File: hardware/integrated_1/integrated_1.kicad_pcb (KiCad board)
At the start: 4 copper layers, 40 x 100 mm, 84 parts, among them J1 USB4105-GF-A-120, J2 HDMI_A_1.4, SW1 DNF, SW2 DNF, U1 XC6SLX9-TQG144, U2 W25Q16JV, U3 RP2040, U5 TPS650250RHBR, Y1 12MHz

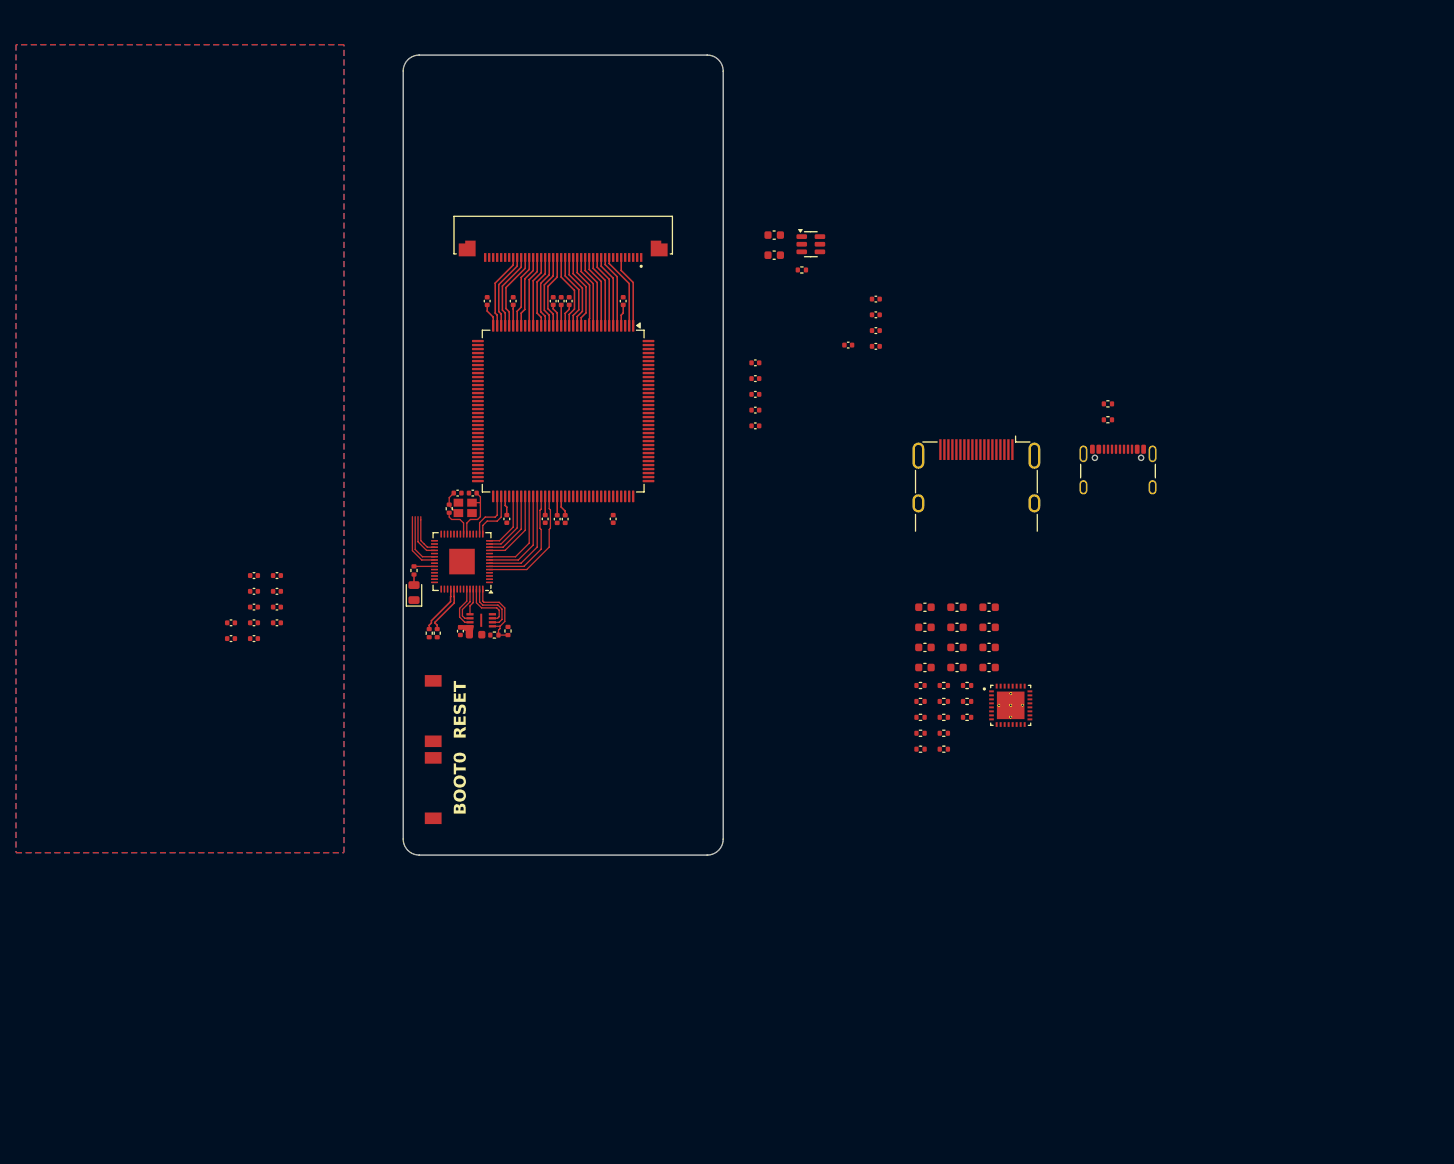
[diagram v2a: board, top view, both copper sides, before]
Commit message: started the layout process + added new hdmi and usb connectors
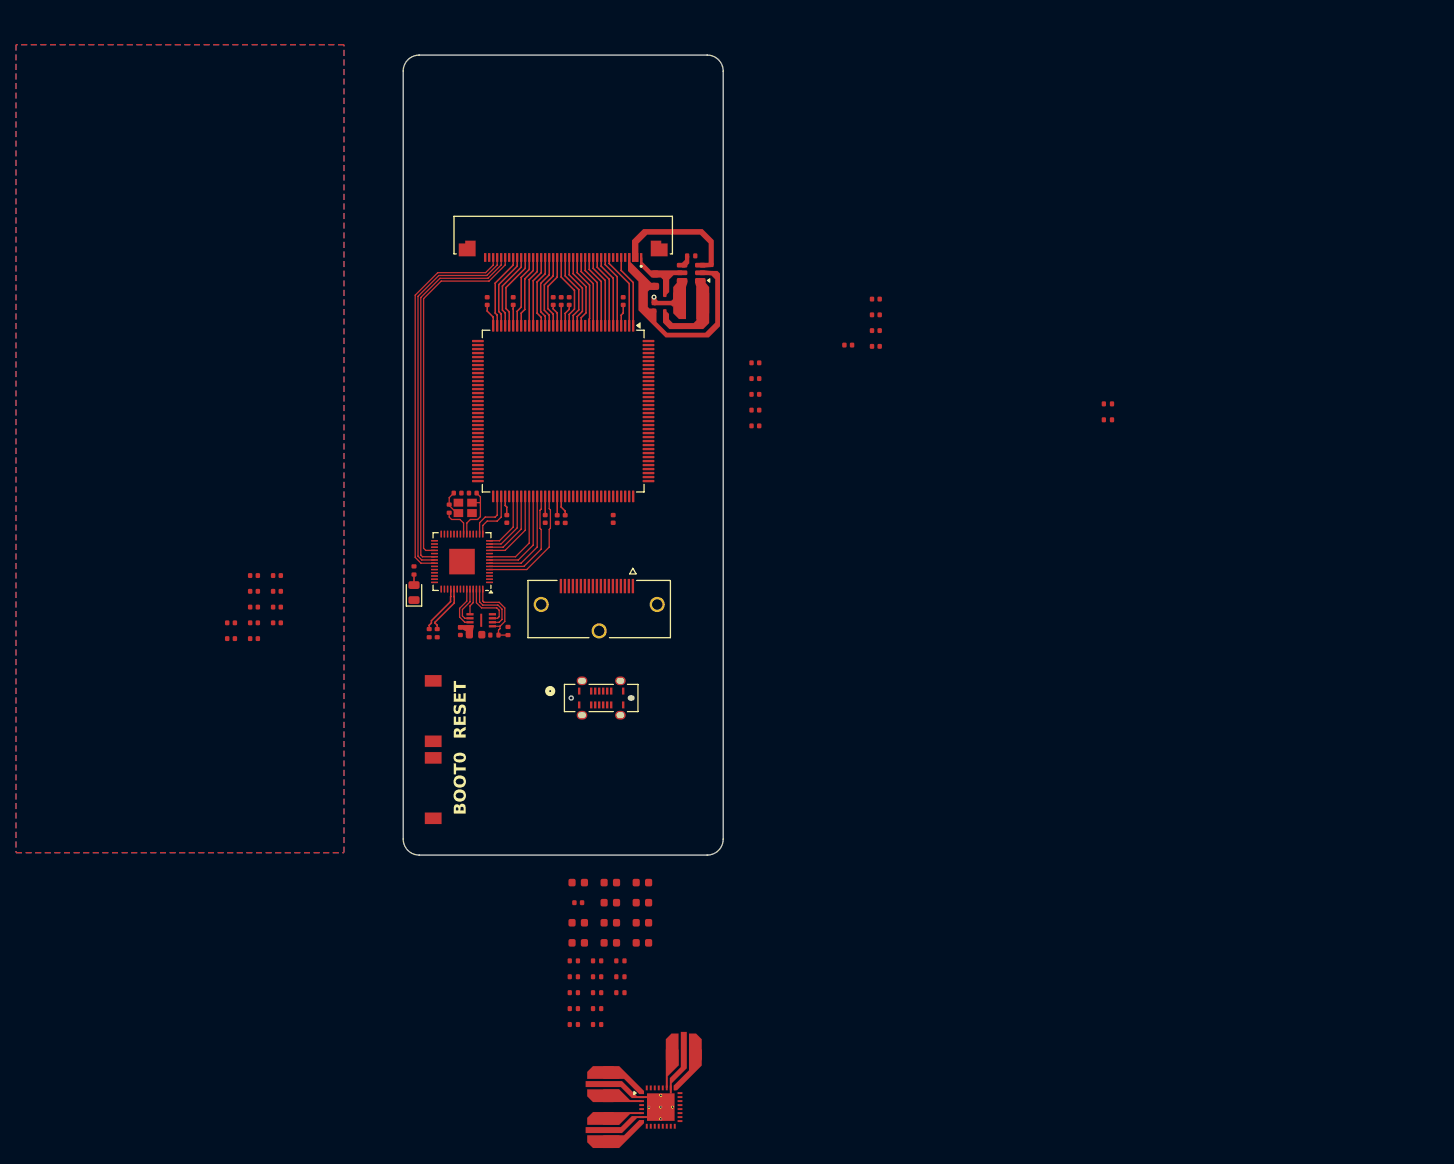
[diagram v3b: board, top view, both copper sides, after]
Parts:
- added D2: ZLLS400TA, Diode_SMD:D_SOD-323, F.Cu at (158.7, 76.5)
- added L1: 22u, KiCAD Library:XRNR4012, F.Cu at (162.0, 76.5)
- added L2: 2u2, KiCAD Library:XRNR4012, F.Cu at (151.0, 179.9)
- added L3: 3u3, KiCAD Library:XRNR4012, F.Cu at (161.1, 169.8)
- added L4: 2u2, KiCAD Library:XRNR4012, F.Cu at (151.0, 174.1)
- added R9: 100, KiCAD Library:R_0402_1005Metric, F.Cu at (162.0, 70.6)
- C1: renamed from C54; footprint Capacitor_SMD:C_0402_1005Metric -> KiCAD Library:C_0402_1005Metric
- C10: renamed from C63; footprint Capacitor_SMD:C_0402_1005Metric -> KiCAD Library:C_0402_1005Metric
- C11: renamed from C1; footprint Capacitor_SMD:C_0402_1005Metric -> KiCAD Library:C_0402_1005Metric
- C12: renamed from C2; footprint Capacitor_SMD:C_0402_1005Metric -> KiCAD Library:C_0402_1005Metric
- C13: renamed from C3; footprint Capacitor_SMD:C_0402_1005Metric -> KiCAD Library:C_0402_1005Metric
- C14: renamed from C4; footprint Capacitor_SMD:C_0402_1005Metric -> KiCAD Library:C_0402_1005Metric
- C15: renamed from C5; footprint Capacitor_SMD:C_0402_1005Metric -> KiCAD Library:C_0402_1005Metric
- C16: renamed from C6; footprint Capacitor_SMD:C_0402_1005Metric -> KiCAD Library:C_0402_1005Metric
- C17: renamed from C7; footprint Capacitor_SMD:C_0402_1005Metric -> KiCAD Library:C_0402_1005Metric
- C18: renamed from C8; footprint Capacitor_SMD:C_0402_1005Metric -> KiCAD Library:C_0402_1005Metric
- C19: renamed from C9; footprint Capacitor_SMD:C_0402_1005Metric -> KiCAD Library:C_0402_1005Metric
- C2: renamed from C55; footprint Capacitor_SMD:C_0402_1005Metric -> KiCAD Library:C_0402_1005Metric
- C20: renamed from C10; footprint Capacitor_SMD:C_0402_1005Metric -> KiCAD Library:C_0402_1005Metric
- C21: renamed from C11; footprint Capacitor_SMD:C_0402_1005Metric -> KiCAD Library:C_0402_1005Metric
- C22: renamed from C12; footprint Capacitor_SMD:C_0402_1005Metric -> KiCAD Library:C_0402_1005Metric
- C23: renamed from C13; footprint Capacitor_SMD:C_0402_1005Metric -> KiCAD Library:C_0402_1005Metric
- C24: renamed from C14; footprint Capacitor_SMD:C_0402_1005Metric -> KiCAD Library:C_0402_1005Metric
- C26: renamed from C16; footprint Capacitor_SMD:C_0402_1005Metric -> KiCAD Library:C_0402_1005Metric
- C27: renamed from C17; footprint Capacitor_SMD:C_0402_1005Metric -> KiCAD Library:C_0402_1005Metric
- C28: renamed from C18; footprint Capacitor_SMD:C_0402_1005Metric -> KiCAD Library:C_0402_1005Metric
- C29: renamed from C19; footprint Capacitor_SMD:C_0402_1005Metric -> KiCAD Library:C_0402_1005Metric
- C3: renamed from C56; footprint Capacitor_SMD:C_0402_1005Metric -> KiCAD Library:C_0402_1005Metric
- C30: renamed from C20; footprint Capacitor_SMD:C_0402_1005Metric -> KiCAD Library:C_0402_1005Metric
- C31: renamed from C21; footprint Capacitor_SMD:C_0402_1005Metric -> KiCAD Library:C_0402_1005Metric
- C32: renamed from C22; footprint Capacitor_SMD:C_0402_1005Metric -> KiCAD Library:C_0402_1005Metric
- C33: renamed from C23; footprint Capacitor_SMD:C_0402_1005Metric -> KiCAD Library:C_0402_1005Metric
- C34: renamed from C24; footprint Capacitor_SMD:C_0402_1005Metric -> KiCAD Library:C_0402_1005Metric
- C35: renamed from C25; footprint Capacitor_SMD:C_0402_1005Metric -> KiCAD Library:C_0402_1005Metric
- C36: renamed from C26; footprint Capacitor_SMD:C_0402_1005Metric -> KiCAD Library:C_0402_1005Metric
- C37: renamed from C27; footprint Capacitor_SMD:C_0603_1608Metric -> KiCAD Library:C_0402_1005Metric
- C38: renamed from C28; footprint Capacitor_SMD:C_0603_1608Metric -> KiCAD Library:C_0603_1608Metric
- C39: renamed from C29; footprint Capacitor_SMD:C_0603_1608Metric -> KiCAD Library:C_0603_1608Metric
- C4: renamed from C57; footprint Capacitor_SMD:C_0402_1005Metric -> KiCAD Library:C_0402_1005Metric
- C40: renamed from C30; footprint Capacitor_SMD:C_0603_1608Metric -> KiCAD Library:C_0402_1005Metric
- C41: renamed from C31; footprint Capacitor_SMD:C_0603_1608Metric -> KiCAD Library:C_0603_1608Metric
- C42: renamed from C32; footprint Capacitor_SMD:C_0603_1608Metric -> KiCAD Library:C_0603_1608Metric
- C43: renamed from C41; footprint Capacitor_SMD:C_0603_1608Metric -> KiCAD Library:C_0603_1608Metric
- C44: renamed from C42; footprint Capacitor_SMD:C_0603_1608Metric -> KiCAD Library:C_0603_1608Metric
- C45: renamed from C35; footprint Capacitor_SMD:C_0603_1608Metric -> KiCAD Library:C_0603_1608Metric
- C46: renamed from C36; footprint Capacitor_SMD:C_0603_1608Metric -> KiCAD Library:C_0603_1608Metric
- C47: renamed from C37; footprint Capacitor_SMD:C_0603_1608Metric -> KiCAD Library:C_0603_1608Metric
- C48: renamed from C38; footprint Capacitor_SMD:C_0603_1608Metric -> KiCAD Library:C_0603_1608Metric
- C49: renamed from C39; footprint Capacitor_SMD:C_0603_1608Metric -> KiCAD Library:C_0603_1608Metric
- C5: renamed from C58; footprint Capacitor_SMD:C_0402_1005Metric -> KiCAD Library:C_0402_1005Metric
- C50: renamed from C40; footprint Capacitor_SMD:C_0603_1608Metric -> KiCAD Library:C_0603_1608Metric
- C6: renamed from C59; footprint Capacitor_SMD:C_0402_1005Metric -> KiCAD Library:C_0402_1005Metric
- C7: renamed from C60; footprint Capacitor_SMD:C_0402_1005Metric -> KiCAD Library:C_0402_1005Metric
- C8: renamed from C61; footprint Capacitor_SMD:C_0402_1005Metric -> KiCAD Library:C_0402_1005Metric
- C9: renamed from C62; footprint Capacitor_SMD:C_0402_1005Metric -> KiCAD Library:C_0402_1005Metric
- J1: footprint Connector_USB:USB_C_Receptacle_GCT_USB4105-xx-A_16P_TopMnt_Horizontal -> KiCAD Library:CONN_217182-0001_MOL
- J2: footprint Connector_HDMI:HDMI_A_Molex_208658-1001_Horizontal -> KiCAD Library:MOLEX_476591102
- R1, R2, R3, R4, R5, R6, R7, R8: footprint Resistor_SMD:R_0402_1005Metric -> KiCAD Library:R_0402_1005Metric
- R10: renamed from R9; footprint Resistor_SMD:R_0402_1005Metric -> KiCAD Library:R_0402_1005Metric
- R11: renamed from R10; footprint Resistor_SMD:R_0402_1005Metric -> KiCAD Library:R_0402_1005Metric
- R12: renamed from R11; footprint Resistor_SMD:R_0402_1005Metric -> KiCAD Library:R_0402_1005Metric
- R13: renamed from R12; footprint Resistor_SMD:R_0402_1005Metric -> KiCAD Library:R_0402_1005Metric
- R14: renamed from R21; footprint Resistor_SMD:R_0402_1005Metric -> KiCAD Library:R_0402_1005Metric
- R15: renamed from R22; footprint Resistor_SMD:R_0402_1005Metric -> KiCAD Library:R_0402_1005Metric
- R16: renamed from R13; footprint Resistor_SMD:R_0402_1005Metric -> KiCAD Library:R_0402_1005Metric
- R17: renamed from R14; footprint Resistor_SMD:R_0402_1005Metric -> KiCAD Library:R_0402_1005Metric
- R18: renamed from R15; footprint Resistor_SMD:R_0402_1005Metric -> KiCAD Library:R_0402_1005Metric
- R19: renamed from R16; footprint Resistor_SMD:R_0402_1005Metric -> KiCAD Library:R_0402_1005Metric
- R20: renamed from R17; footprint Resistor_SMD:R_0402_1005Metric -> KiCAD Library:R_0402_1005Metric
- R21: renamed from R18; footprint Resistor_SMD:R_0402_1005Metric -> KiCAD Library:R_0402_1005Metric
- R22: renamed from R19; footprint Resistor_SMD:R_0402_1005Metric -> KiCAD Library:R_0402_1005Metric
- R23: renamed from R20; footprint Resistor_SMD:R_0402_1005Metric -> KiCAD Library:R_0402_1005Metric
- U4: value ~ -> AP5725
- moved J1 70.2 mm to (150.8, 125.9)
- moved U5 66.6 mm to (158.2, 177.0)
- moved C45 55.3 mm to (151.9, 148.9)
- moved C47 55.3 mm to (151.9, 154.0)
- moved C48 55.3 mm to (151.9, 156.5)
- moved C46 55.3 mm to (151.9, 151.4)
- moved C39 55.3 mm to (147.9, 148.9)
- moved C41 55.3 mm to (147.9, 154.0)
- moved C42 55.3 mm to (147.9, 156.5)
- moved C43 55.3 mm to (155.9, 154.0)
- moved C44 55.3 mm to (155.9, 156.5)
- moved C49 55.3 mm to (155.9, 148.9)
- moved R11 55.3 mm to (147.3, 158.7)
- moved R12 55.3 mm to (147.3, 160.7)
- moved R13 55.3 mm to (147.3, 162.7)
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- renumbered C15 to C25
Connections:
- C1 pad 1: /VCC_{AUX} -> /VCC_{INT}
- C2 pad 1: /VCC_{AUX} -> /VCC_{INT}
- C3 pad 1: /VCC_{AUX} -> /VCC_{INT}
- C4 pad 1: /VCC_{AUX} -> /VCC_{INT}
- C43 pad 1: /VCC_{AUX} -> /VCC_{INT}
- C44 pad 1: /VCC_{AUX} -> /VCC_{INT}
- C5 pad 1: /VCC_{AUX} -> /VCC_{INT}
- R14 pad 1: /VCC_{AUX} -> /VCC_{INT}
- U1 pad 129: /VCC_{AUX} -> /VCC_{INT}
- U1 pad 20: /VCC_{AUX} -> /VCC_{INT}
- U1 pad 36: /VCC_{AUX} -> /VCC_{INT}
- U1 pad 53: /VCC_{AUX} -> /VCC_{INT}
- U1 pad 90: /VCC_{AUX} -> /VCC_{INT}
- U3 pad 31: /TP_SDA -> unconnected-(U3-GPIO20-Pad31)
- U3 pad 32: /TP_SCL -> /TP_INT
- U3 pad 34: /TP_RST -> /TP_SDA
- U3 pad 35: /TP_INT -> /TP_SCL
- U3 pad 36: unconnected-(U3-GPIO24-Pad36) -> /TP_RST
- U4 pad 1: Net-(D2-A) -> /Backlight/SW
- U4 pad 4: /BL_PWM -> Net-(U4-EN)
- U5 pad 27: Net-(U5-L2) -> /Buck Converter/L2
- U5 pad 3: Net-(U5-L3) -> /Buck Converter/L3
- U5 pad 6: Net-(U5-L1) -> /Buck Converter/L1
- U5 pad 8: /VCC_{AUX} -> /VCC_{INT}
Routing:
- net /TP_SDA: track 5.05 -> 46.7 mm
- net /TP_SCL: track 5.65 -> 47.2 mm
- net /TP_RST: track 6.89 -> 47.7 mm
- net /TP_INT: track 7.49 -> 45.6 mm
- net /VCC_{INT}: track 0.00 -> 8.30 mm
- net /VCC_{AUX}: track 13.3 -> 4.97 mm
- net /RP2040/LED_STATUS: track 2.56 -> 0.00 mm
- net +5V: vias 0 -> 1
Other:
- board text added: "Display cable goes here"

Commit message: significant progress in the layout has been made, close to completion
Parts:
- removed the C45 at (151.9, 148.9)
- removed the R16 at (147.3, 164.7)
- removed the R17 at (147.3, 166.7)
- added C1: 100n, KiCAD Library:C_0402_1005Metric, F.Cu at (158.7, 67.6)
- added C2: 1u, KiCAD Library:C_0402_1005Metric, F.Cu at (158.7, 66.7)
- added C24: 100n, KiCAD Library:C_0402_1005Metric, F.Cu at (185.6, 96.3)
- added C40: 100n, KiCAD Library:C_0402_1005Metric, F.Cu at (168.8, 126.6)
- added D1: LED, KiCAD Library:D_0805_2012Metric, F.Cu at (158.2, 82.8)
- added D2: LED, KiCAD Library:D_0805_2012Metric, F.Cu at (158.2, 84.8)
- added D3: LED, KiCAD Library:D_0805_2012Metric, F.Cu at (158.2, 86.8)
- added D4: LED, KiCAD Library:D_0805_2012Metric, F.Cu at (158.2, 88.8)
- added D5: LED, KiCAD Library:D_0805_2012Metric, F.Cu at (158.2, 80.8)
- added D6: LED, KiCAD Library:D_0805_2012Metric, F.Cu at (158.2, 78.8)
- added D7: LED, KiCAD Library:D_0805_2012Metric, F.Cu at (158.2, 76.8)
- added D8: LED, KiCAD Library:D_0805_2012Metric, F.Cu at (158.2, 74.8)
- added G*** (x2): LOGO, LOGO, F.Cu at (184.8, 120.0)
- added G***: LOGO, LOGO, F.Cu at (189.8, 110.0)
- added J3: DEBUG, Paw-Connect:Paw-Connect_RevB_TC2030-IDC-NL_2x03_P1.27mm_Vertical, F.Cu at (166.9, 137.0)
- added JP1: SolderJumper_2_Open, Jumper:SolderJumper-2_P1.3mm_Open_RoundedPad1.0x1.5mm, F.Cu at (188.6, 94.7)
- added JP2: SolderJumper_2_Open, Jumper:SolderJumper-2_P1.3mm_Open_RoundedPad1.0x1.5mm, F.Cu at (188.6, 92.2)
- added JP3: SolderJumper_2_Open, Jumper:SolderJumper-2_P1.3mm_Open_RoundedPad1.0x1.5mm, F.Cu at (188.6, 89.7)
- added JP4: SolderJumper_2_Open, Jumper:SolderJumper-2_P1.3mm_Open_RoundedPad1.0x1.5mm, F.Cu at (188.6, 87.2)
- added JP5: SolderJumper_2_Open, Jumper:SolderJumper-2_P1.3mm_Open_RoundedPad1.0x1.5mm, F.Cu at (188.6, 84.7)
- added JP6: SolderJumper_2_Open, Jumper:SolderJumper-2_P1.3mm_Open_RoundedPad1.0x1.5mm, F.Cu at (188.6, 82.2)
- added JP7: SolderJumper_2_Open, Jumper:SolderJumper-2_P1.3mm_Open_RoundedPad1.0x1.5mm, F.Cu at (188.6, 79.7)
- added JP8: SolderJumper_2_Open, Jumper:SolderJumper-2_P1.3mm_Open_RoundedPad1.0x1.5mm, F.Cu at (188.6, 77.2)
- added R10: 270, KiCAD Library:R_0402_1005Metric, F.Cu at (156.2, 106.1)
- added R9: 1k, KiCAD Library:R_0402_1005Metric, F.Cu at (169.3, 133.7)
- added RN1: 270, KiCAD Library:C_ARRAY_EXB28V_PAN-L, F.Cu at (159.0, 91.2)
- added RN2: 270, KiCAD Library:C_ARRAY_EXB28V_PAN-L, F.Cu at (159.0, 72.2)
- added SW1: DNF, KiCAD Library:PTS636 SM25J SMTR LFS, F.Cu at (157.8, 55.5)
- added U2: IS25LP128F-JBLE-TR, Package_SO:SOIC-8_5.275x5.275mm_P1.27mm, F.Cu at (188.2, 99.6)
- added U5: FT24C04A, Package_SO:SOIC-8_3.9x4.9mm_P1.27mm, F.Cu at (166.8, 130.0)
- D9: renamed from D1; footprint Diode_SMD:D_0805_2012Metric -> KiCAD Library:D_0805_2012Metric
- DS1: footprint KiCAD Library:AMPHENOL_F32Q-1A7H1-11040 -> KiCAD Library:GCT_FFC2B35-40-G_REVA2
- R8: value 270 -> 1k
- moved C32 59.3 mm to (166.5, 107.8)
- moved D9 58.4 mm to (184.8, 123.0)
- moved C36 58.2 mm to (168.0, 103.2)
- moved C30 56.7 mm to (157.7, 98.8), turned to 180 degrees
- moved R19 55.5 mm to (188.1, 120.1), turned to 180 degrees
- moved R18 55.5 mm to (190.1, 120.1), turned to 180 degrees
- moved C29 55.3 mm to (159.6, 111.7), turned to -90 degrees
- moved C31 53.1 mm to (160.4, 111.7), turned to -90 degrees
- moved L3 53.0 mm to (189.2, 124.9)
- moved L4 52.3 mm to (177.9, 129.3)
- moved U7 52.1 mm to (185.7, 132.7)
- moved C13 51.8 mm to (186.2, 82.4)
- moved R15 51.6 mm to (190.7, 134.8), turned to 90 degrees
- moved C35 51.5 mm to (158.7, 113.5), turned to 90 degrees
- moved L2 51.3 mm to (177.9, 136.2)
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- renumbered C8 to C10, C9 to C11, C10 to C12, C11 to C13, C12 to C14, C13 to C15, C14 to C16, C15 to C17, C16 to C18, C17 to C19, C18 to C20, C19 to C21, C20 to C22, C21 to C23, C22 to C25, C23 to C26, C24 to C27, C25 to C28, C26 to C29, C1 to C3, C27 to C30, C28 to C31, C29 to C32, C30 to C33, C31 to C34, C32 to C35, C33 to C36, C34 to C37, C35 to C38, C36 to C39, C2 to C4, C37 to C41, C38 to C42, C39 to C43, C40 to C44, C41 to C45, C42 to C46, C43 to C47, C44 to C48, C46 to C49, C3 to C5, C47 to C50, C48 to C51, C49 to C52, C50 to C53, C4 to C6, C5 to C7, C6 to C8, C7 to C9, D2 to D10, R9 to R11, R10 to R12, R11 to R13, R12 to R14, R13 to R15, R14 to R16, R15 to R17, SW1 to SW2, SW2 to SW3, U2 to U3, U3 to U4, U4 to U6, U5 to U7
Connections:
- net Net-(J1-CC1) renamed /CC_{1}
- net Net-(J1-CC2) renamed /CC_{2}
- net Net-(U5-DEFDCDC1) renamed /Buck Converter/FB_{DCDC_{1}}
- net Net-(U5-VCC) renamed /Buck Converter/VCC_RC
- C13 pad 1: +3V3 -> /FPGA IO Bank A/FPGA_{BANK0}
- C14 pad 1: +3V3 -> /FPGA IO Bank A/FPGA_{BANK0}
- C15 pad 1: +3V3 -> /FPGA IO Bank A/FPGA_{BANK0}
- C16 pad 1: +3V3 -> /FPGA IO Bank A/FPGA_{BANK1}
- C17 pad 1: +3V3 -> /FPGA IO Bank A/FPGA_{BANK1}
- C18 pad 1: +3V3 -> /FPGA IO Bank A/FPGA_{BANK1}
- C19 pad 1: +3V3 -> /FPGA IO Bank B/FPGA_{BANK2}
- C20 pad 1: +3V3 -> /FPGA IO Bank B/FPGA_{BANK2}
- C21 pad 1: +3V3 -> /FPGA IO Bank B/FPGA_{BANK3}
- C22 pad 1: +3V3 -> /FPGA IO Bank B/FPGA_{BANK3}
- C23 pad 1: +3V3 -> /FPGA IO Bank B/FPGA_{BANK3}
- D9 pad 2: Net-(D1-A) -> Net-(D9-A)
- J2 pad SH1: (no net) -> GND
- J2 pad SH2: (no net) -> GND
- J2 pad SH3: (no net) -> GND
- R8 pad 1: Net-(D1-A) -> +3V3
- R8 pad 2: /RP2040/LED_STATUS -> /RP2040/EEPROM_SDA
- U1 pad 103: +3V3 -> /FPGA IO Bank A/FPGA_{BANK1}
- U1 pad 111: /FPGA IO Bank A/GPIO1_25 -> unconnected-(U1A-IO_L66N_SCP0_0-Pad111)
- U1 pad 112: /FPGA IO Bank A/GPIO1_24 -> unconnected-(U1A-IO_L66P_SCP1_0-Pad112)
- U1 pad 114: /FPGA IO Bank A/GPIO1_23 -> unconnected-(U1A-IO_L65N_SCP2_0-Pad114)
- U1 pad 115: /FPGA IO Bank A/GPIO1_22 -> unconnected-(U1A-IO_L65P_SCP3_0-Pad115)
- U1 pad 116: /FPGA IO Bank A/GPIO1_21 -> unconnected-(U1A-IO_L64N_SCP4_0-Pad116)
- U1 pad 117: /FPGA IO Bank A/GPIO1_20 -> unconnected-(U1A-IO_L64P_SCP5_0-Pad117)
- U1 pad 118: /FPGA IO Bank A/GPIO1_19 -> unconnected-(U1A-IO_L63N_SCP6_0-Pad118)
- U1 pad 119: /FPGA IO Bank A/GPIO1_18 -> unconnected-(U1A-IO_L63P_SCP7_0-Pad119)
- U1 pad 120: /FPGA IO Bank A/GPIO1_17 -> unconnected-(U1A-IO_L62N_VREF_0-Pad120)
- U1 pad 121: /FPGA IO Bank A/GPIO1_16 -> unconnected-(U1A-IO_L62P_0-Pad121)
- U1 pad 122: +3V3 -> /FPGA IO Bank A/FPGA_{BANK0}
- U1 pad 123: /FPGA IO Bank A/GPIO1_15 -> unconnected-(U1A-IO_L37N_GCLK12_0-Pad123)
- U1 pad 124: /FPGA IO Bank A/GPIO1_14 -> unconnected-(U1A-IO_L37P_GCLK13_0-Pad124)
- U1 pad 125: +3V3 -> /FPGA IO Bank A/FPGA_{BANK0}
- U1 pad 126: /FPGA IO Bank A/GPIO1_13 -> unconnected-(U1A-IO_L36N_GCLK14_0-Pad126)
- U1 pad 127: /FPGA IO Bank A/GPIO1_12 -> unconnected-(U1A-IO_L36P_GCLK15_0-Pad127)
- U1 pad 131: /FPGA IO Bank A/GPIO1_11 -> unconnected-(U1A-IO_L35N_GCLK16_0-Pad131)
- U1 pad 132: /FPGA IO Bank A/GPIO1_10 -> unconnected-(U1A-IO_L35P_GCLK17_0-Pad132)
- U1 pad 133: /FPGA IO Bank A/GPIO1_09 -> unconnected-(U1A-IO_L34N_GCLK18_0-Pad133)
- U1 pad 134: /FPGA IO Bank A/GPIO1_08 -> unconnected-(U1A-IO_L34P_GCLK19_0-Pad134)
- U1 pad 135: +3V3 -> /FPGA IO Bank A/FPGA_{BANK0}
- U1 pad 137: /FPGA IO Bank A/GPIO1_07 -> unconnected-(U1A-IO_L4N_0-Pad137)
- U1 pad 138: /FPGA IO Bank A/GPIO1_06 -> unconnected-(U1A-IO_L4P_0-Pad138)
- U1 pad 139: /FPGA IO Bank A/GPIO1_05 -> unconnected-(U1A-IO_L3N_0-Pad139)
- U1 pad 140: /FPGA IO Bank A/GPIO1_04 -> unconnected-(U1A-IO_L3P_0-Pad140)
- U1 pad 141: /FPGA IO Bank A/GPIO1_03 -> unconnected-(U1A-IO_L2N_0-Pad141)
- U1 pad 142: /FPGA IO Bank A/GPIO1_02 -> unconnected-(U1A-IO_L2P_0-Pad142)
- U1 pad 143: /FPGA IO Bank A/GPIO1_01 -> unconnected-(U1A-IO_L1N_VREF_0-Pad143)
- U1 pad 144: /FPGA IO Bank A/GPIO1_00 -> unconnected-(U1A-IO_L1P_HSWAPEN_0-Pad144)
- U1 pad 18: +3V3 -> /FPGA IO Bank B/FPGA_{BANK3}
- U1 pad 31: +3V3 -> /FPGA IO Bank B/FPGA_{BANK3}
- U1 pad 37: unconnected-(U1C-PROGRAM_B_2-Pad37) -> /FPGA JTAG/FPGA_RST
- U1 pad 38: /FPGA IO Bank B/GPIO0_25 -> /FPGA IO Bank B/LED7
- U1 pad 39: /FPGA IO Bank B/GPIO0_24 -> /FPGA IO Bank B/LED6
- U1 pad 4: +3V3 -> /FPGA IO Bank B/FPGA_{BANK3}
- U1 pad 40: /FPGA IO Bank B/GPIO0_23 -> /FPGA IO Bank B/LED5
- U1 pad 41: /FPGA IO Bank B/GPIO0_22 -> /FPGA IO Bank B/LED4
- U1 pad 42: +3V3 -> /FPGA IO Bank B/FPGA_{BANK2}
- U1 pad 43: /FPGA IO Bank B/GPIO0_21 -> /FPGA IO Bank B/LED3
- U1 pad 44: /FPGA IO Bank B/GPIO0_20 -> /FPGA IO Bank B/LED2
- U1 pad 45: /FPGA IO Bank B/GPIO0_19 -> /FPGA IO Bank B/LED1
- U1 pad 46: /FPGA IO Bank B/GPIO0_18 -> /FPGA IO Bank B/LED0
- U1 pad 47: /FPGA IO Bank B/GPIO0_17 -> unconnected-(U1B-IO_L48N_RDWR_B_VREF_2-Pad47)
- U1 pad 48: /FPGA IO Bank B/GPIO0_16 -> unconnected-(U1B-IO_L48P_D7_2-Pad48)
- U1 pad 50: /FPGA IO Bank B/GPIO0_15 -> unconnected-(U1B-IO_L31N_GCLK30_D15_2-Pad50)
- U1 pad 51: /FPGA IO Bank B/GPIO0_14 -> unconnected-(U1B-IO_L31P_GCLK31_D14_2-Pad51)
- U1 pad 55: /FPGA IO Bank B/GPIO0_13 -> unconnected-(U1B-IO_L30N_GCLK0_USERCCLK_2-Pad55)
- U1 pad 56: /FPGA IO Bank B/GPIO0_12 -> unconnected-(U1B-IO_L30P_GCLK1_D13_2-Pad56)
- U1 pad 57: /FPGA IO Bank B/GPIO0_11 -> unconnected-(U1B-IO_L14N_D12_2-Pad57)
- U1 pad 58: /FPGA IO Bank B/GPIO0_10 -> unconnected-(U1B-IO_L14P_D11_2-Pad58)
- U1 pad 59: /FPGA IO Bank B/GPIO0_09 -> unconnected-(U1B-IO_L13N_D10_2-Pad59)
- U1 pad 60: /FPGA IO Bank B/GPIO0_08 -> unconnected-(U1B-IO_L13P_M1_2-Pad60)
- U1 pad 61: /FPGA IO Bank B/GPIO0_07 -> unconnected-(U1B-IO_L12N_D2_MISO3_2-Pad61)
- U1 pad 62: /FPGA IO Bank B/GPIO0_06 -> unconnected-(U1B-IO_L12P_D1_MISO2_2-Pad62)
- U1 pad 63: +3V3 -> /FPGA IO Bank B/FPGA_{BANK2}
- U1 pad 64: /FPGA IO Bank B/GPIO0_05 -> unconnected-(U1B-IO_L3N_MOSI_CSI_B_MISO0_2-Pad64)
- U1 pad 65: /FPGA IO Bank B/GPIO0_04 -> unconnected-(U1B-IO_L3P_D0_DIN_MISO_MISO1_2-Pad65)
- U1 pad 66: /FPGA IO Bank B/GPIO0_03 -> unconnected-(U1B-IO_L2N_CMPMOSI_2-Pad66)
- U1 pad 67: /FPGA IO Bank B/GPIO0_02 -> unconnected-(U1B-IO_L2P_CMPCLK_2-Pad67)
- U1 pad 69: /FPGA IO Bank B/GPIO0_01 -> unconnected-(U1B-IO_L1N_M0_CMPMISO_2-Pad69)
- U1 pad 70: /FPGA IO Bank B/GPIO0_00 -> unconnected-(U1B-IO_L1P_CCLK_2-Pad70)
- U1 pad 73: unconnected-(U1C-SUSPEND-Pad73) -> GND
- U1 pad 76: +3V3 -> /FPGA IO Bank A/FPGA_{BANK1}
- U1 pad 86: +3V3 -> /FPGA IO Bank A/FPGA_{BANK1}
- U4 pad 40: unconnected-(U3-GPIO28_ADC2-Pad40) -> /RP2040/EEPROM_SCL
- U4 pad 41: unconnected-(U3-GPIO29_ADC3-Pad41) -> /RP2040/EEPROM_SDA
- U7 pad 10: +1V8 -> unconnected-(U7-FB_LDO2-Pad10)
- U7 pad 14: +1V8 -> unconnected-(U7-VLDO2-Pad14)
- U7 pad 34: (no net) -> GND
- U7 pad 35: (no net) -> GND
- U7 pad 36: (no net) -> GND
- U7 pad 37: (no net) -> GND
- U7 pad 38: (no net) -> GND
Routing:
- net /BL_PWM: track 0.00 -> 109.1 mm, vias 0 -> 2
- net /Buck Converter/~{PWR_FAIL}: track 0.00 -> 66.3 mm, vias 0 -> 2
- net /Buck Converter/EN: track 0.00 -> 64.8 mm, vias 0 -> 2
- net /RP2040/SWD: track 0.00 -> 64.2 mm, vias 0 -> 2
- net /RP2040/SWCLK: track 0.00 -> 59.7 mm, vias 0 -> 2
- net Net-(D9-A): track 0.00 -> 45.8 mm, vias 0 -> 2
- net GND: track 0.00 -> 44.1 mm, vias 0 -> 61
- net /DVI_UTIL: track 0.00 -> 40.8 mm, vias 0 -> 2
- net /TMS: track 0.00 -> 39.5 mm, vias 0 -> 2
- net /RP2040/DEBUG_UART_TX: track 0.00 -> 39.5 mm, vias 0 -> 2
- net /TDI: track 0.00 -> 37.8 mm, vias 0 -> 2
- net /RP2040/DEBUG_UART_RX: track 0.00 -> 37.4 mm, vias 0 -> 2
- net +3V3: track 12.9 -> 50.0 mm, vias 0 -> 22
- net /RP2040/EEPROM_SDA: track 0.00 -> 37.0 mm
- net /TDO: track 0.00 -> 36.6 mm, vias 0 -> 2
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- added copper zone on In2.Cu, net +2V5
- added copper zone on In2.Cu, net +3V3
- added copper zone on B.Cu, net +5V
- added copper zone on In2.Cu, net +5V
- added copper zone on B.Cu, net /FPGA IO Bank A/FPGA_{BANK0}
- added copper zone on B.Cu, net /FPGA IO Bank A/FPGA_{BANK1}
- added copper zone on B.Cu, net /FPGA IO Bank B/FPGA_{BANK2}
- added copper zone on B.Cu, net /FPGA IO Bank B/FPGA_{BANK3}
- added copper zone on In2.Cu, net /VCC_{AUX}
- added copper zone on In2.Cu, net /VCC_{INT}
- removed copper zone on In2.Cu, net GND
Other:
- board text added: "0"
- board text added: "1"
- board text added: "2"
- board text added: "2V5"
- board text added: "3"
- board text added: "3V3"
- board text added: "4"
- board text added: "5"
- board text added: "6"
- board text added: "7"
- board text added: "V_{CCO_{0}}"
- board text added: "V_{CCO_{1}}"
- board text added: "V_{CCO_{2}}"
- board text added: "V_{CCO_{3}}"
